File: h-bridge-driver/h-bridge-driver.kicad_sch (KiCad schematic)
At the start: 34 parts, among them J1 CON_HDR_100MILS_M_TH_2X8, J2 CON_HDR_100MILS_M_TH_1X3, J3 CON_TERM_BLK_1X2_TB008A-508-0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, Q1 TRX_2NPN_BC846S,115, Q2 TRX_NMOS_PJD40N04_L2_00001, Q3 TRX_NMOS_PJD40N04_L2_00001, Q4 TRX_NMOS_PJD40N04_L2_00001, Q5 TRX_NMOS_PJD40N04_L2_00001, U1 DRV_A4957SESTR-T

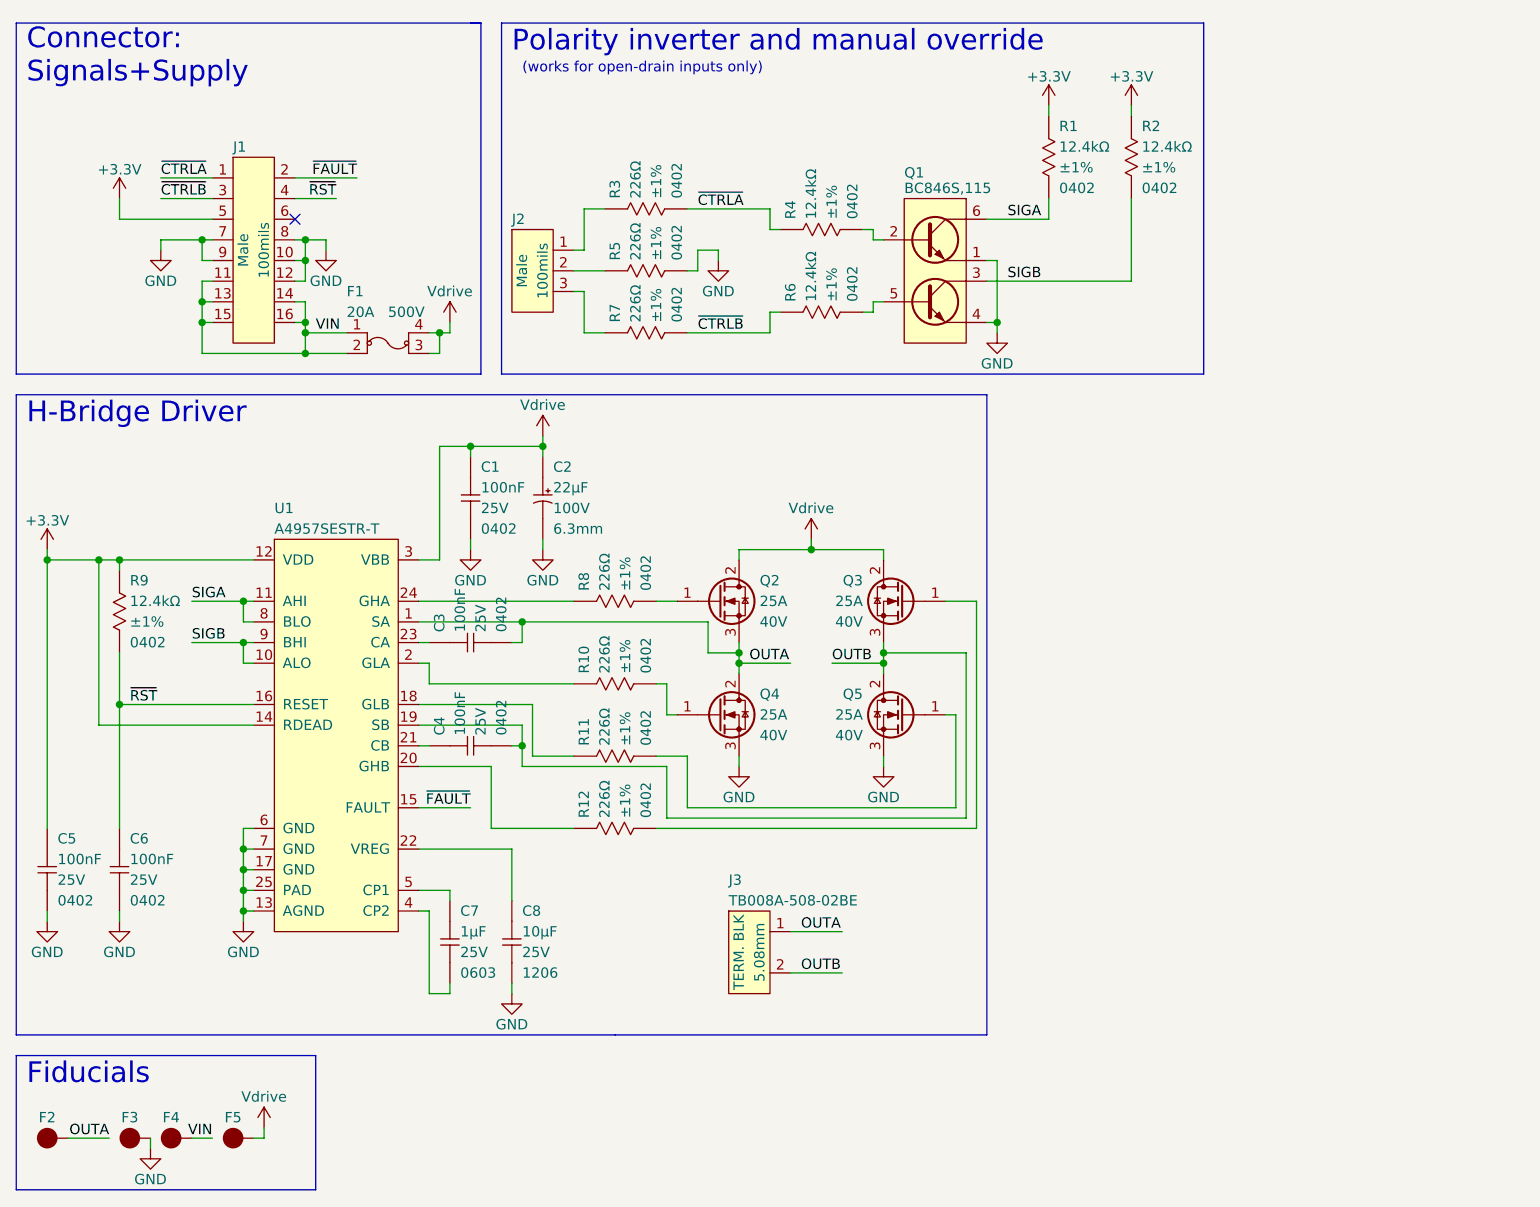
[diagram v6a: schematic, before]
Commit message: Add LEDs, fix NMOS, Add logos and infos on PCBs.
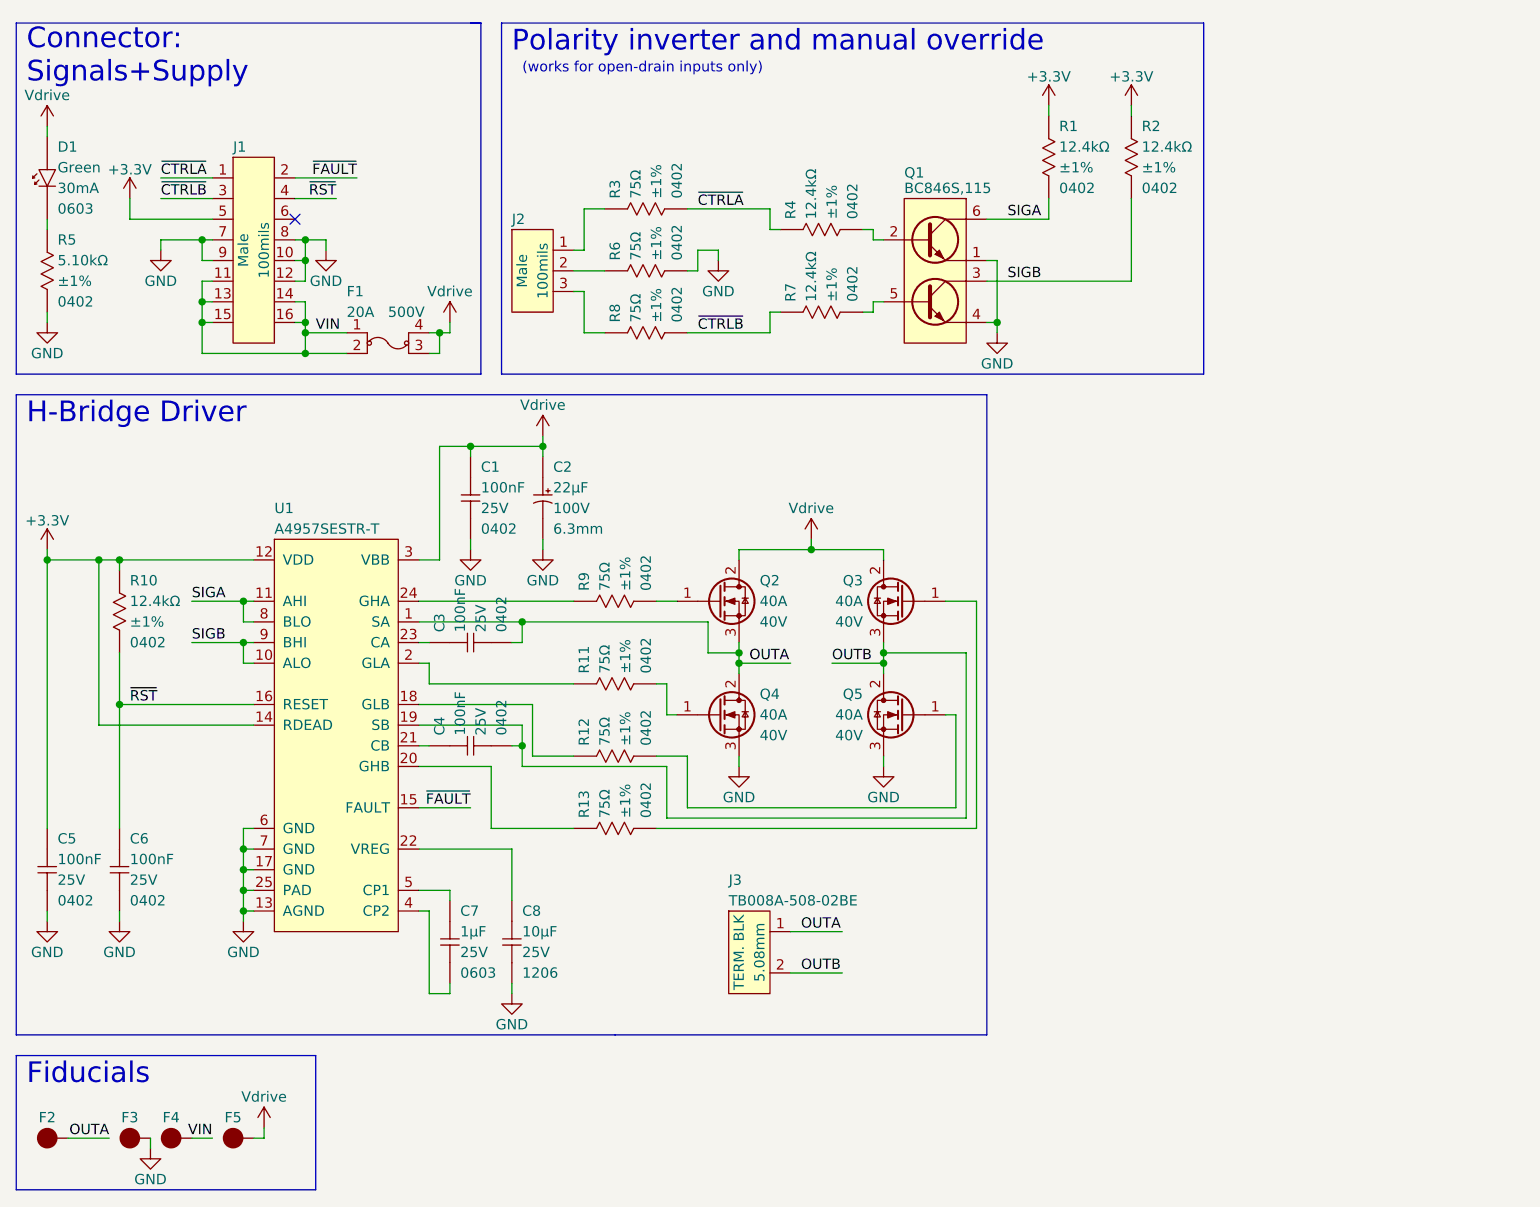
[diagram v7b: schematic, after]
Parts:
- added D1: DIO_LED_GREEN_150060GS75000, connaxio-diodes:LED_0603_1608M, symbol connaxio-diodes:DIO_LED_GREEN_150060GS75000
- added R5: RES_5.10KΩ_1%_0402, connaxio-resistors:RES_0402_1005M, symbol connaxio-resistors:RES_5.10KΩ_1%_0402
- Q2, Q3, Q4, Q5: Current 25A -> 40A; Manufacturer Alpha & Omega Semiconductor Inc. -> Panjit International Inc.; Manufacturer Part Number AOD4189 -> PJD40N04_L2_00001
- R11: renamed from R10; symbol connaxio-resistors:RES_226Ω_1%_0402 -> connaxio-resistors:RES_75Ω_1%_0402; Manufacturer Part Number RMCF0402FT226R -> RMCF0402FT75R0; Property 226Ω -> 75Ω
- R12: renamed from R11; symbol connaxio-resistors:RES_226Ω_1%_0402 -> connaxio-resistors:RES_75Ω_1%_0402; Manufacturer Part Number RMCF0402FT226R -> RMCF0402FT75R0; Property 226Ω -> 75Ω
- R13: renamed from R12; symbol connaxio-resistors:RES_226Ω_1%_0402 -> connaxio-resistors:RES_75Ω_1%_0402; Manufacturer Part Number RMCF0402FT226R -> RMCF0402FT75R0; Property 226Ω -> 75Ω
- R3: symbol connaxio-resistors:RES_226Ω_1%_0402 -> connaxio-resistors:RES_75Ω_1%_0402; Manufacturer Part Number RMCF0402FT226R -> RMCF0402FT75R0; Property 226Ω -> 75Ω
- R6: renamed from R5; symbol connaxio-resistors:RES_226Ω_1%_0402 -> connaxio-resistors:RES_75Ω_1%_0402; Manufacturer Part Number RMCF0402FT226R -> RMCF0402FT75R0; Property 226Ω -> 75Ω
- R8: renamed from R7; symbol connaxio-resistors:RES_226Ω_1%_0402 -> connaxio-resistors:RES_75Ω_1%_0402; Manufacturer Part Number RMCF0402FT226R -> RMCF0402FT75R0; Property 226Ω -> 75Ω
- R9: renamed from R8; symbol connaxio-resistors:RES_226Ω_1%_0402 -> connaxio-resistors:RES_75Ω_1%_0402; Manufacturer Part Number RMCF0402FT226R -> RMCF0402FT75R0; Property 226Ω -> 75Ω
- renumbered R9 to R10, R6 to R7
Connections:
- net GND: now also R5.2
- net Vdrive: now also D1.2 (A)
- new net: D1.1 (K), R5.1

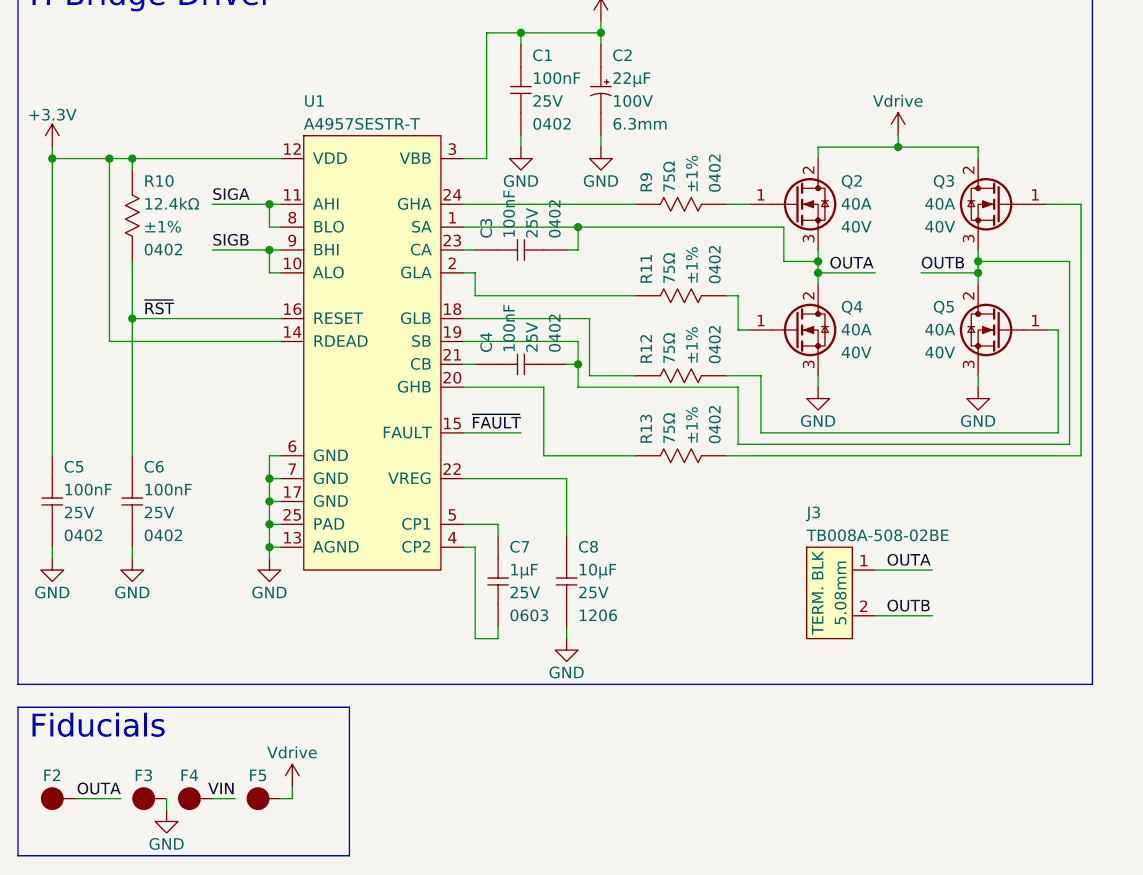
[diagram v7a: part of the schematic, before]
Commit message: Add Enclosure piercing guide and fix h-bridge-driver NMOS pads.
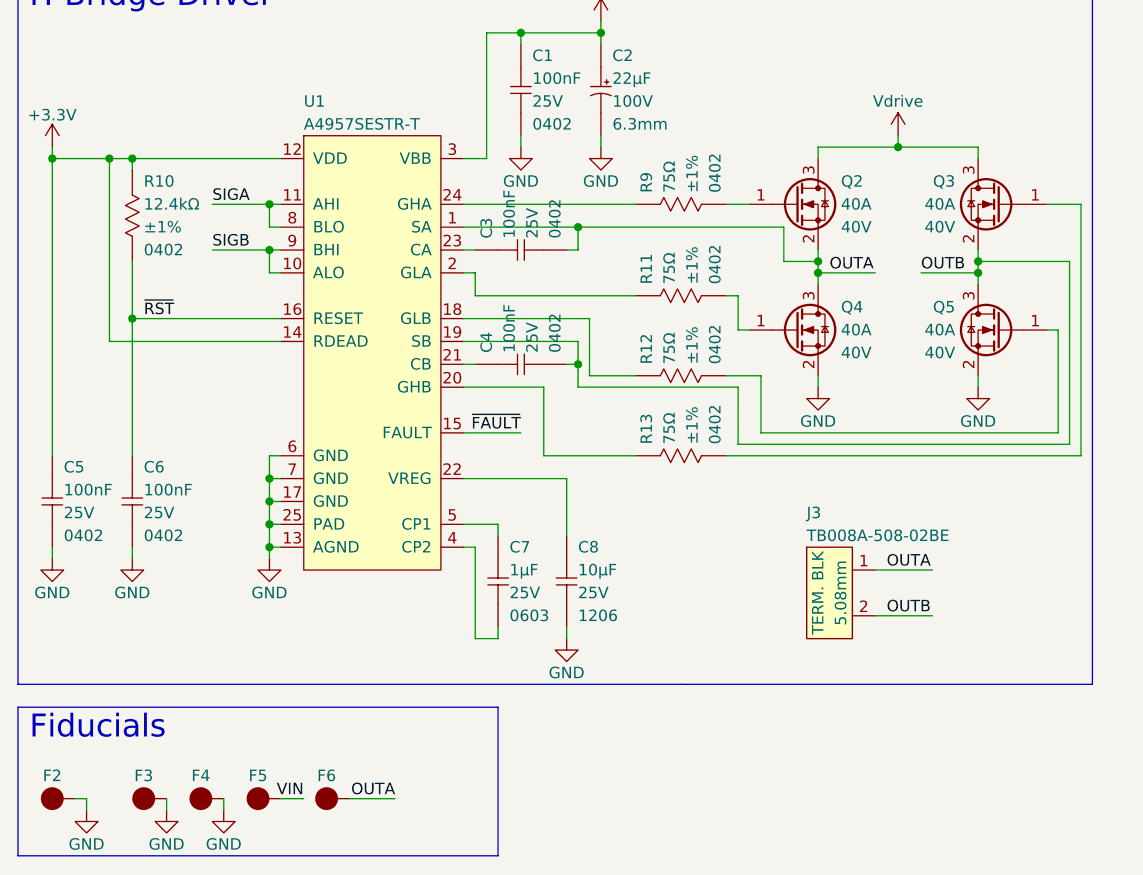
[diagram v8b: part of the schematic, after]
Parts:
- added F4: FID_1X1, connaxio-mechanical:FID_1X1, symbol connaxio-mechanical:FID_1X1
- renumbered F4 to F5, F5 to F6
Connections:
- net GND: now also F2.1, Q4.2 (S), Q5.2 (S), F4.1; no longer Q4.3 (S), Q5.3 (S)
- net OUTA: now also F6.1, Q2.2 (S), Q4.3 (D); no longer F2.1, Q2.3 (S), Q4.2 (D)
- net OUTB: now also Q3.2 (S), Q5.3 (D); no longer Q3.3 (S), Q5.2 (D)
- net Vdrive: now also Q2.3 (D), Q3.3 (D); no longer F6.1, Q2.2 (D), Q3.2 (D)
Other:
- moved on the sheet: F5, F6
